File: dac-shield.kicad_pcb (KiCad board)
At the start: 2 copper layers, 53.3 x 53.3 mm, 46 parts, among them J1 Conn_01x02, J2 Conn_01x02, J3 Conn_01x02, J4 Conn_01x02, J5 Conn_01x02, J6 Conn_01x02, J7 Conn_01x02, J8 Conn_01x02

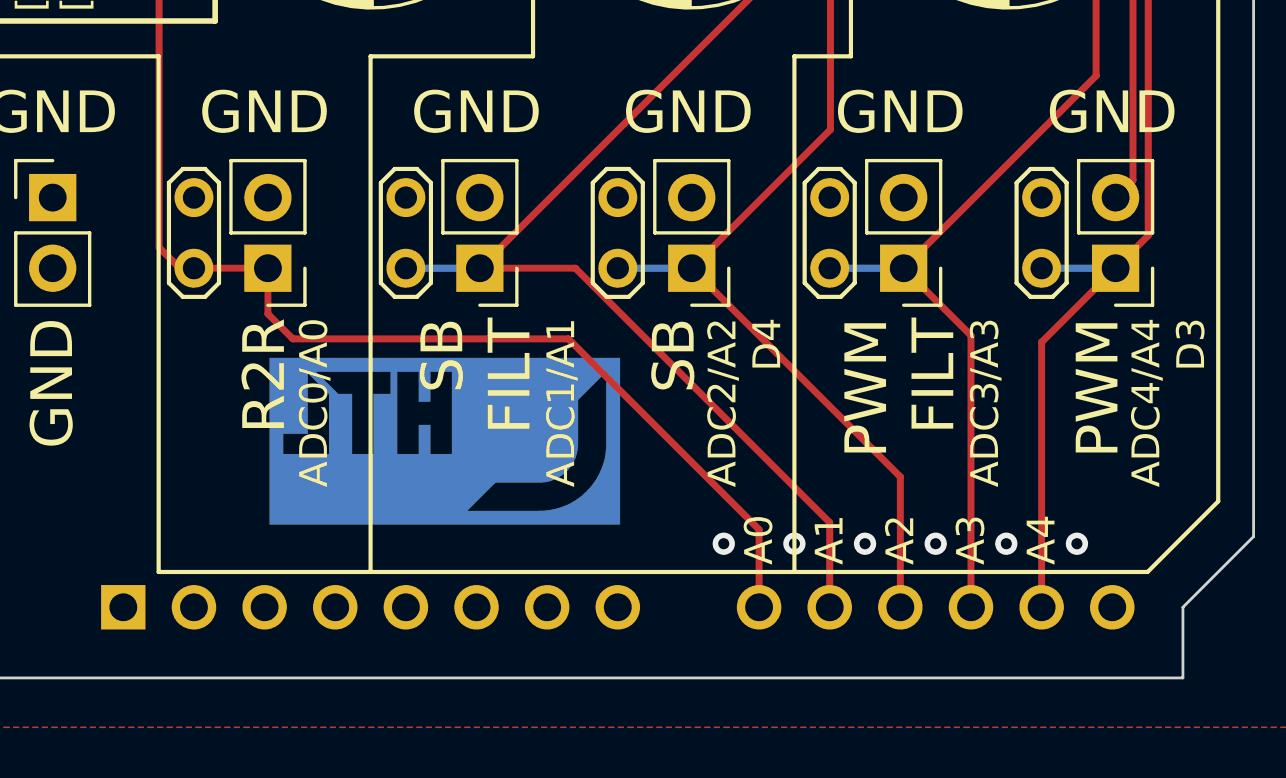
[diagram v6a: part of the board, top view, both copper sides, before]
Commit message: changed testpoint footprints
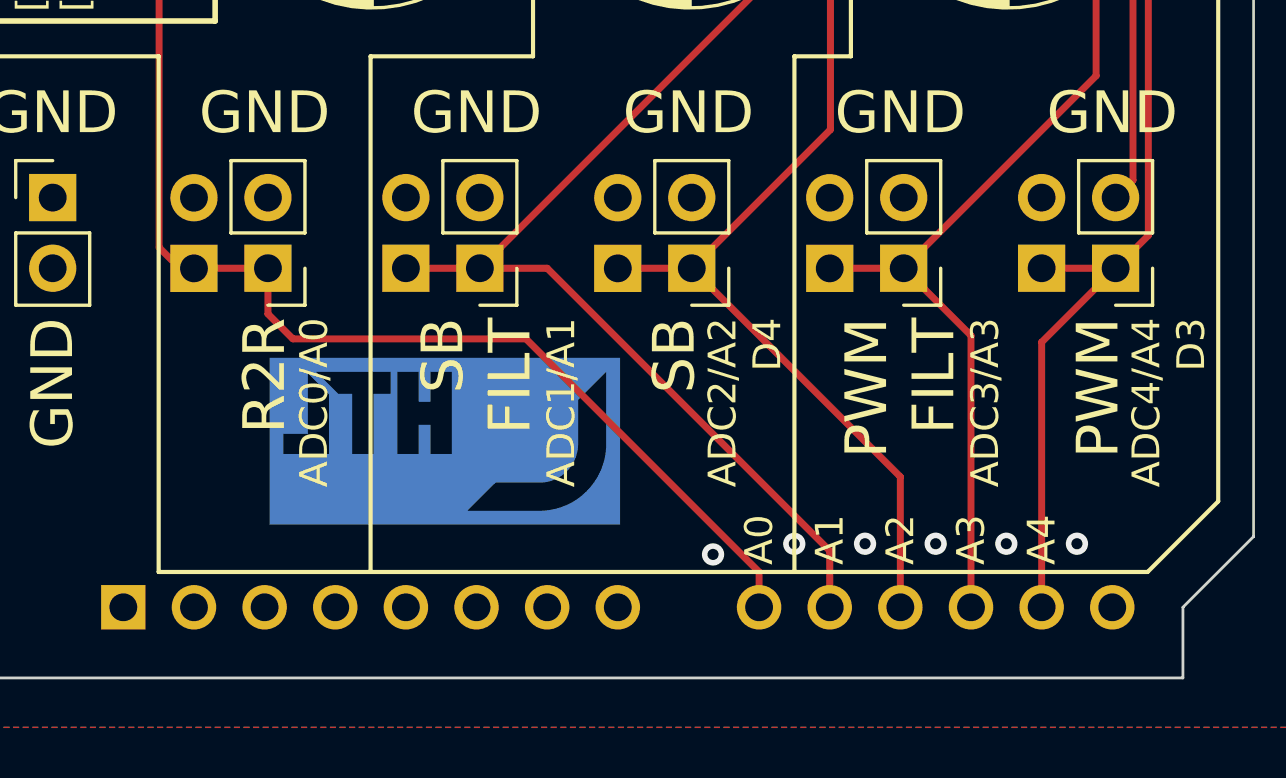
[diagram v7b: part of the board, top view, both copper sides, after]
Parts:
- TP1, TP2, TP3, TP4, TP5: footprint TestPoint:TestPoint_2Pads_Pitch2.54mm_Drill0.8mm -> Connector_PinHeader_2.54mm:PinHeader_1x02_P2.54mm_Vertical
- turned TP1 to 180 degrees
- turned TP3 to 180 degrees
- turned TP4 to 180 degrees
- turned TP2 to 180 degrees
- turned TP5 to 180 degrees
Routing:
- net r2r_filt: track 59.9 -> 59.0 mm
- net sb_filt: track 58.9 -> 58.3 mm

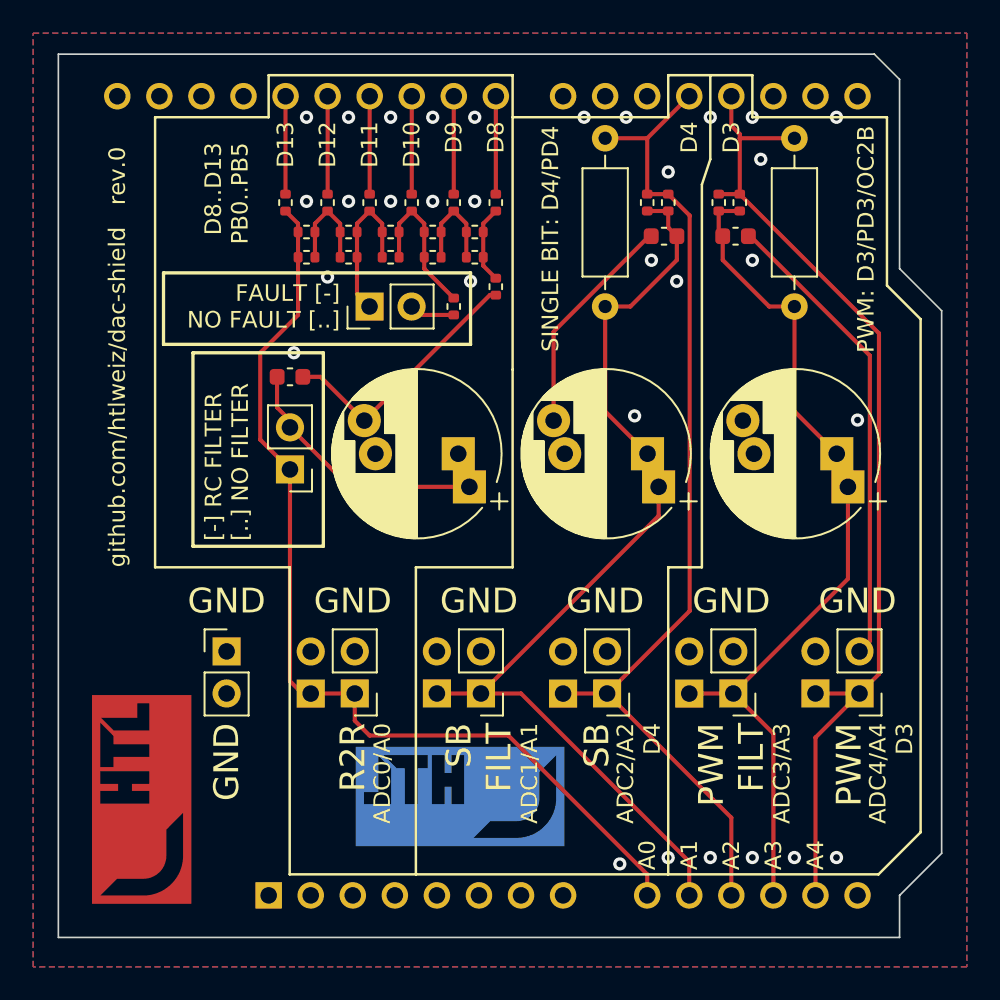
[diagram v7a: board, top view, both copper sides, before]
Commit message: created footprint options
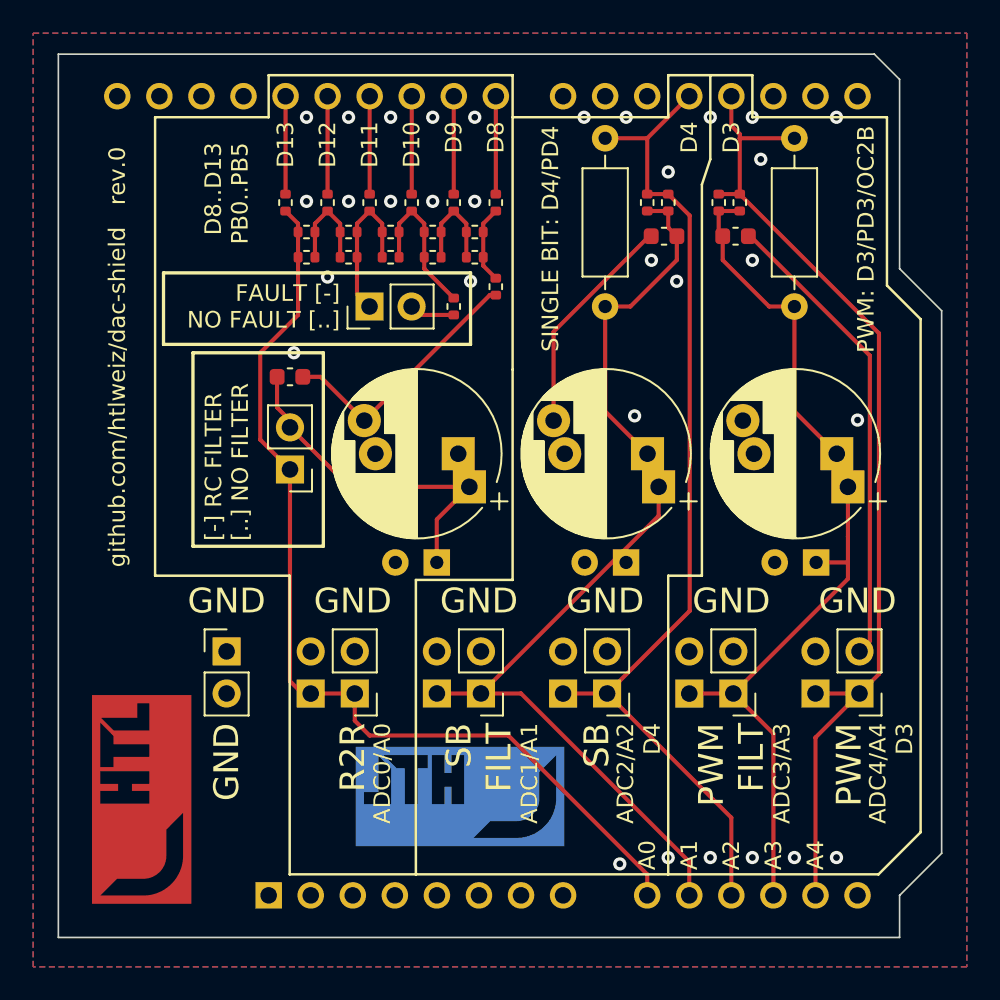
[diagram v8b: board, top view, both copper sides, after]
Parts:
- added C3: dnp/4u7, Capacitor_THT:CP_Radial_D5.0mm_P2.50mm, F.Cu at (155.0, 106.9)
- added C7: dnp/4u7, Capacitor_THT:CP_Radial_D5.0mm_P2.50mm, F.Cu at (132.1, 106.9)
- added C9: dnp/4u7, Capacitor_THT:CP_Radial_D5.0mm_P2.50mm, F.Cu at (143.5, 106.9)
- renumbered C5 to C4, C6 to C5, C3 to C6, C4 to C8, J8 to J1, J1 to J2, J2 to J3, J3 to J5, J5 to J8, R18 to R15, R19 to R16, R20 to R17, R21 to R18, R22 to R19, R23 to R20, R24 to R21, R15 to R22, R16 to R23, R17 to R24
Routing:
- net Net-(C4-Pad1): track 15.7 -> 21.1 mm
- net pwm_filt: track 51.0 -> 52.9 mm
